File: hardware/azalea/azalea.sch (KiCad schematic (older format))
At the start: 88 parts, among them J1 NEIGHBOR1, J2 NEIGHBOR2, J3 USB-MICRO-B-SHIELDED, J4 USB-MICRO-B-SHIELDED, J5 JTAG, J7 BONUS_ROW, SW1 DFU, SW2 RESET, U1 LPC4330FBD144, U2 W25Q16DV, U3 AP7333, U4 IP4220CZ6, U5 NX5P2553GV, X1 XTAL4PIN, X2 RTC_XTAL

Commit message: max current note
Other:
- note added: "Maximum current: 300 mA"
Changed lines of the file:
@@
 Text Label 14050 6350 1    40   ~ 0
 USB1_SHIELD
+Text Notes 2000 7250 0    60   ~ 0
+Maximum current: 300 mA
 $EndSCHEMATC

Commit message: fixed some 0603 modules that should have been 0805
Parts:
- C11, C4, FB1, FB2, FB3: footprint gsg-modules:0603 -> gsg-modules:0805
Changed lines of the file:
@@
 F 0 "FB1" H 3950 5600 50  0000 C CNN
 F 1 "FILTER" H 3950 5350 50  0000 C CNN
-F 2 "gsg-modules:0603" H 3950 5450 60  0001 C CNN
+F 2 "gsg-modules:0805" H 3950 5450 60  0001 C CNN
 F 3 "" H 3950 5450 60  0000 C CNN
 F 4 "Murata" H 3950 5450 60  0001 C CNN "Manufacturer"
@@
 F 0 "C4" H 3725 7200 50  0000 L CNN
 F 1 "10uF" H 3725 7000 50  0000 L CNN
-F 2 "gsg-modules:0603" H 3738 6950 30  0001 C CNN
+F 2 "gsg-modules:0805" H 3738 6950 30  0001 C CNN
 F 3 "" H 3700 7100 60  0000 C CNN
 F 4 "Murata" H 3700 7100 60  0001 C CNN "Manufacturer"
@@
 F 0 "C11" H 13675 3450 50  0000 L CNN
 F 1 "10uF" H 13675 3250 50  0000 L CNN
-F 2 "gsg-modules:0603" H 13688 3200 30  0001 C CNN
+F 2 "gsg-modules:0805" H 13688 3200 30  0001 C CNN
 F 3 "" H 13650 3350 60  0000 C CNN
 F 4 "Murata" H 13650 3350 60  0001 C CNN "Manufacturer"
@@
 F 0 "FB2" H 3050 4700 50  0000 C CNN
 F 1 "FILTER" H 3050 4450 50  0000 C CNN
-F 2 "gsg-modules:0603" H 3050 4550 60  0001 C CNN
+F 2 "gsg-modules:0805" H 3050 4550 60  0001 C CNN
 F 3 "" H 3050 4550 60  0000 C CNN
 F 4 "Murata" H 3050 4550 60  0001 C CNN "Manufacturer"
@@
 F 0 "FB3" H 13600 6550 50  0000 C CNN
 F 1 "FILTER" H 13600 6300 50  0000 C CNN
-F 2 "gsg-modules:0603" H 13600 6400 60  0001 C CNN
+F 2 "gsg-modules:0805" H 13600 6400 60  0001 C CNN
 F 3 "" H 13600 6400 60  0000 C CNN
 F 4 "Murata" H 13600 6400 60  0001 C CNN "Manufacturer"
@@
 	5850 5500 5000 5500
 Wire Wire Line
-	5000 5200 5000 5500
+	5000 5500 5000 5200
 Wire Wire Line
 	5750 5800 5850 5800
@@
 	4300 5450 4900 5450
 Wire Wire Line
-	4900 6850 4900 5450
+	4900 5450 4900 6850
 Wire Wire Line
 	3700 6850 3700 6950
@@
 	5850 5700 4800 5700
 Wire Wire Line
-	4800 5000 4800 5700
+	4800 5700 4800 5000
 Wire Wire Line
-	2800 5000 4800 5000
+	4800 5000 2800 5000
 Wire Wire Line
 	2800 4900 2900 4900
@@
 	5850 4800 5250 4800
 Wire Wire Line
-	5250 4150 5250 4800
+	5250 4800 5250 4150
 Wire Wire Line
-	4900 4150 5250 4150
+	5250 4150 4900 4150
 Wire Wire Line
 	5850 4700 5350 4700
@@
 Connection ~ 3450 6750
 Wire Wire Line
-	3350 6850 4900 6850
+	4900 6850 3350 6850
 Connection ~ 3700 6850
 Wire Wire Line
@@
 	5850 6600 5500 6600
 Wire Wire Line
-	5500 8800 5500 6600
+	5500 6600 5500 8800
 Wire Wire Line
-	4000 8800 5500 8800
+	5500 8800 4000 8800
 Wire Wire Line
 	4200 9000 4000 9000
 Wire Wire Line
-	5200 8000 5200 6300
+	5200 6300 5200 8000
 Wire Wire Line
-	3950 8000 5200 8000
+	5200 8000 3950 8000
 Wire Wire Line
 	4450 8000 4450 7900
@@
 USB1_D+
 Wire Wire Line
-	2800 5200 5000 5200
+	5000 5200 2800 5200
 Connection ~ 3050 5200
 Wire Wire Line

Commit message: changed 47 pF caps to 18 pF for bom reduction
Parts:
- C8, C9: Description CAP CER 47PF 50V 5% NP0 0603 -> CAP CER 18PF 50V 5% NP0 0603; Part Number GRM1885C1H470JA01D -> GRM1885C1H180JA01D
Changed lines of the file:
@@
 F 3 "" H 12500 5750 60  0000 C CNN
 F 4 "Murata" H 12500 5750 60  0001 C CNN "Manufacturer"
-F 5 "GRM1885C1H470JA01D" H 12500 5750 60  0001 C CNN "Part Number"
-F 6 "CAP CER 47PF 50V 5% NP0 0603" H 12500 5750 60  0001 C CNN "Description"
+F 5 "GRM1885C1H180JA01D" H 12500 5750 60  0001 C CNN "Part Number"
+F 6 "CAP CER 18PF 50V 5% NP0 0603" H 12500 5750 60  0001 C CNN "Description"
 	1    12500 5750
 	1    0    0    -1
@@
 F 3 "" H 12150 5750 60  0000 C CNN
 F 4 "Murata" H 12150 5750 60  0001 C CNN "Manufacturer"
-F 5 "GRM1885C1H470JA01D" H 12150 5750 60  0001 C CNN "Part Number"
-F 6 "CAP CER 47PF 50V 5% NP0 0603" H 12150 5750 60  0001 C CNN "Description"
+F 5 "GRM1885C1H180JA01D" H 12150 5750 60  0001 C CNN "Part Number"
+F 6 "CAP CER 18PF 50V 5% NP0 0603" H 12150 5750 60  0001 C CNN "Description"
 	1    12150 5750
 	1    0    0    -1

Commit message: RTC XTAL is no longer DNP
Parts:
- C1, C2, X2: Note DNP -> (none)
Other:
- note added: "bonus row is optional for neighbors"
- note removed: "bonus row may not make it onto final layout"
- note removed: "optional RTC section"
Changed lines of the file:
@@
 F 5 "GRM1885C1H180JA01D" H 2000 8900 60  0001 C CNN "Part Number"
 F 6 "CAP CER 18PF 50V 5% NP0 0603" H 2000 8900 60  0001 C CNN "Description"
-F 7 "DNP" H 1900 8800 60  0000 C CNN "Note"
 	1    2000 8900
 	1    0    0    -1
@@
 F 5 "GRM1885C1H180JA01D" H 1500 8900 60  0001 C CNN "Part Number"
 F 6 "CAP CER 18PF 50V 5% NP0 0603" H 1500 8900 60  0001 C CNN "Description"
-F 7 "DNP" H 1400 8800 60  0000 C CNN "Note"
 	1    1500 8900
 	1    0    0    -1
@@
 F 5 "AB26TRQ-32.768KHZ-T" H 1750 8550 60  0001 C CNN "Part Number"
 F 6 "CRYSTAL 32.768KHZ 12.5PF SMD" H 1750 8550 60  0001 C CNN "Description"
-F 7 "DNP" H 1750 8300 60  0000 C CNN "Note"
 	1    1750 8550
 	1    0    0    -1
@@
 Text Notes 14750 7750 1    40   ~ 0
 BOOT
-Text Notes 14150 6800 0    60   ~ 0
-bonus row may not make it onto final layout
+Text Notes 14300 6800 0    60   ~ 0
+bonus row is optional for neighbors
 Wire Wire Line
 	7500 8250 7500 8050
@@
 Text Notes 3250 1000 0    60   ~ 0
 boot selection
-Text Notes 1250 8250 0    60   ~ 0
-optional RTC section
 Text Notes 8350 8900 0    60   ~ 0
 test points

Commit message: azalea: made USB connectors protrude less from PCB edge, lengthened pads to ease soldering
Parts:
- J3, J4: footprint gsg-modules:USB-MICROB-FCI-10103592-EXT -> gsg-modules:USB-MICROB-FCI-10103592-LONGPADS
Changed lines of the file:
@@
 F 0 "J3" H 2700 5400 60  0000 C CNN
 F 1 "USB-MICRO-B-SHIELDED" V 2950 5100 60  0000 C CNN
-F 2 "gsg-modules:USB-MICROB-FCI-10103592-EXT" H 2550 5100 60  0001 C CNN
+F 2 "gsg-modules:USB-MICROB-FCI-10103592-LONGPADS" H 2550 5100 60  0001 C CNN
 F 3 "" H 2550 5100 60  0000 C CNN
 F 4 "FCI" H 2550 5100 60  0001 C CNN "Manufacturer"
@@
 F 0 "J4" H 13950 5800 60  0000 C CNN
 F 1 "USB-MICRO-B-SHIELDED" V 14200 5500 60  0000 C CNN
-F 2 "gsg-modules:USB-MICROB-FCI-10103592-EXT" H 13800 5500 60  0001 C CNN
+F 2 "gsg-modules:USB-MICROB-FCI-10103592-LONGPADS" H 13800 5500 60  0001 C CNN
 F 3 "" H 13800 5500 60  0000 C CNN
 F 4 "FCI" H 13800 5500 60  0001 C CNN "Manufacturer"

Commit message: extended crystal pads for easier soldering
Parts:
- X1: footprint gsg-modules:XTAL3.2x2.5mm -> gsg-modules:XTAL3.2x2.5mm-EXT
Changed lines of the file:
@@
 F 0 "X1" H 4600 4300 60  0000 C CNN
 F 1 "XTAL4PIN" H 4600 4000 60  0000 C CNN
-F 2 "gsg-modules:XTAL3.2x2.5mm" H 4600 4150 60  0001 C CNN
+F 2 "gsg-modules:XTAL3.2x2.5mm-EXT" H 4600 4150 60  0001 C CNN
 F 3 "" H 4600 4150 60  0000 C CNN
 F 4 "TXC" H 4600 4150 60  0001 C CNN "Manufacturer"

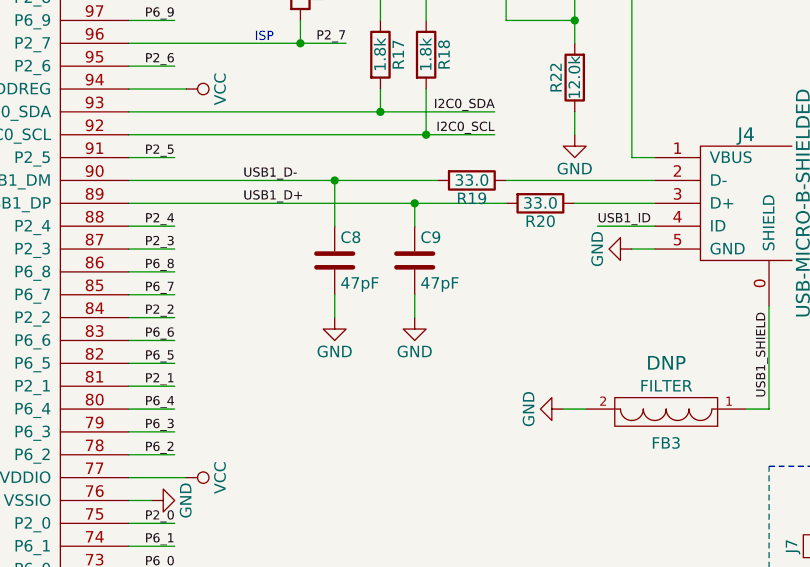
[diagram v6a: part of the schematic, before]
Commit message: azalea: corrected value of 47 pF caps that were changed to 18 pF
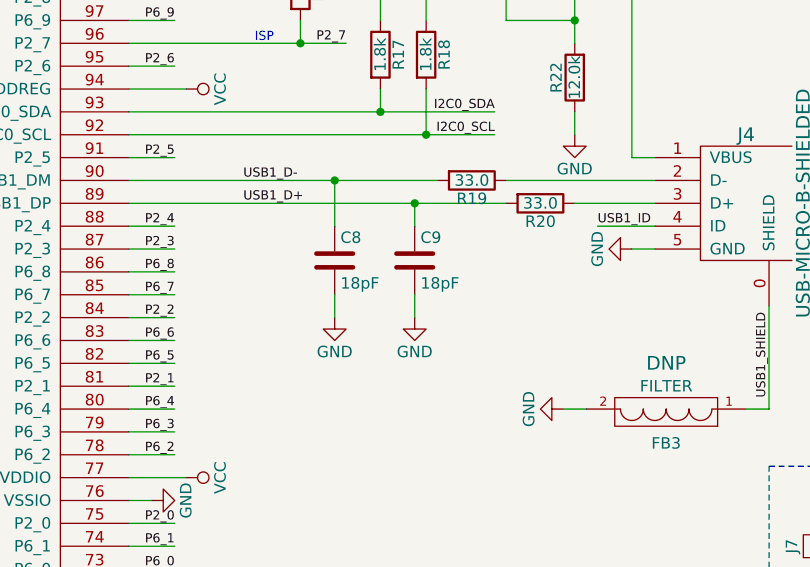
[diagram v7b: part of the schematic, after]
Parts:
- C8, C9: value 47pF -> 18pF
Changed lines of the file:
@@
 P 12500 5750
 F 0 "C9" H 12525 5850 50  0000 L CNN
-F 1 "47pF" H 12525 5650 50  0000 L CNN
+F 1 "18pF" H 12525 5650 50  0000 L CNN
 F 2 "gsg-modules:0603" H 12538 5600 30  0001 C CNN
 F 3 "" H 12500 5750 60  0000 C CNN
@@
 P 12150 5750
 F 0 "C8" H 12175 5850 50  0000 L CNN
-F 1 "47pF" H 12175 5650 50  0000 L CNN
+F 1 "18pF" H 12175 5650 50  0000 L CNN
 F 2 "gsg-modules:0603" H 12188 5600 30  0001 C CNN
 F 3 "" H 12150 5750 60  0000 C CNN

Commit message: azalea: LED part selection
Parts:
- D1, D3: Description (none) -> LED GREEN DIFFUSED 0603 SMD; Manufacturer (none) -> Lumex; Part Number (none) -> SML-LX0603GW-TR
- D2, D4: Description (none) -> LED YELLOW DIFFUSED 0603 SMD; Manufacturer (none) -> Lumex; Part Number (none) -> SML-LX0603YW-TR
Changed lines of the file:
@@
 F 2 "gsg-modules:0603D" H 1150 3500 60  0001 C CNN
 F 3 "" H 1150 3500 60  0000 C CNN
+F 4 "Lumex" H 1150 3500 60  0001 C CNN "Manufacturer"
+F 5 "SML-LX0603GW-TR" H 1150 3500 60  0001 C CNN "Part Number"
+F 6 "LED GREEN DIFFUSED 0603 SMD" H 1150 3500 60  0001 C CNN "Description"
 	1    1150 3500
 	0    -1   -1   0
@@
 F 2 "gsg-modules:0603D" H 1450 3500 60  0001 C CNN
 F 3 "" H 1450 3500 60  0000 C CNN
+F 4 "Lumex" H 1450 3500 60  0001 C CNN "Manufacturer"
+F 5 "SML-LX0603YW-TR" H 1450 3500 60  0001 C CNN "Part Number"
+F 6 "LED YELLOW DIFFUSED 0603 SMD" H 1450 3500 60  0001 C CNN "Description"
 	1    1450 3500
 	0    -1   -1   0
@@
 F 2 "gsg-modules:0603D" H 1750 3500 60  0001 C CNN
 F 3 "" H 1750 3500 60  0000 C CNN
+F 4 "Lumex" H 1750 3500 60  0001 C CNN "Manufacturer"
+F 5 "SML-LX0603GW-TR" H 1750 3500 60  0001 C CNN "Part Number"
+F 6 "LED GREEN DIFFUSED 0603 SMD" H 1750 3500 60  0001 C CNN "Description"
 	1    1750 3500
 	0    -1   -1   0
@@
 F 2 "gsg-modules:0603D" H 2050 3500 60  0001 C CNN
 F 3 "" H 2050 3500 60  0000 C CNN
+F 4 "Lumex" H 2050 3500 60  0001 C CNN "Manufacturer"
+F 5 "SML-LX0603YW-TR" H 2050 3500 60  0001 C CNN "Part Number"
+F 6 "LED YELLOW DIFFUSED 0603 SMD" H 2050 3500 60  0001 C CNN "Description"
 	1    2050 3500
 	0    -1   -1   0
